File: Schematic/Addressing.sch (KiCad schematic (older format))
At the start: 5 parts, among them IC10 74LS593, IC11 74HCT251, IC7 74HCT574, IC8 74HCT574, IC9 74LS593

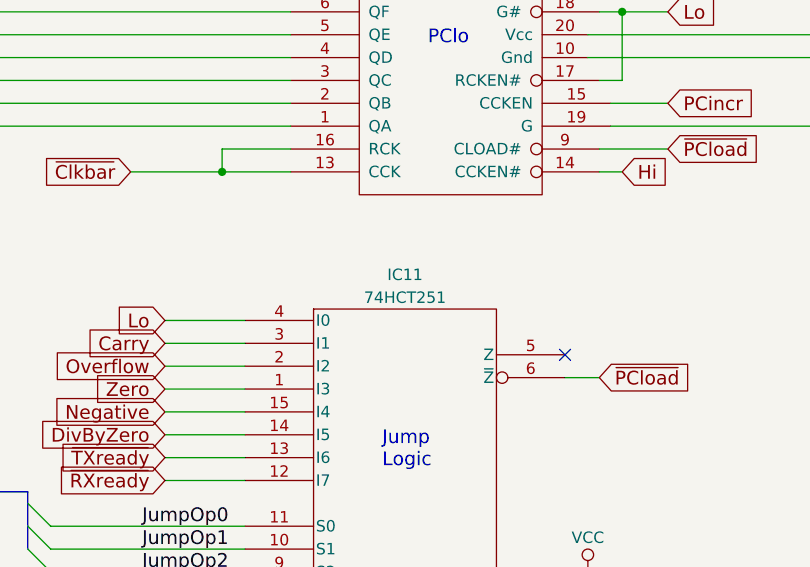
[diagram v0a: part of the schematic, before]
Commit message: Brought the PCB up to date with the new schematic, and tested the RAM with a test program.
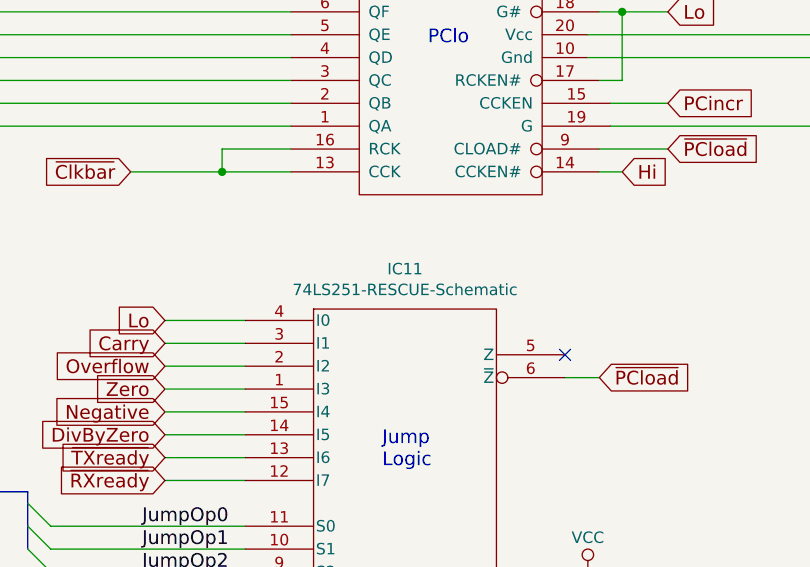
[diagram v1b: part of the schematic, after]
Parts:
- IC11: value 74HCT251 -> 74LS251-RESCUE-Schematic; footprint Housings_DIP:DIP-16_W7.62mm_Socket -> Package_DIP:DIP-16_W7.62mm_Socket
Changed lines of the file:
@@
 Text GLabel 7800 1350 2    60   Input ~ 0
 ~Reset
-$Comp
-L Schematic-rescue:74LS251-RESCUE-Schematic U?
-U 1 1 5CA1932F
-P 6150 5400
-AR Path="/5CA1932F" Ref="U?"  Part="1"
-AR Path="/5C985077/5CA1932F" Ref="IC11"  Part="1"
-F 0 "IC11" H 6150 6250 50  0000 C CNN
-F 1 "74HCT251" H 6150 6150 50  0000 C CNN
-F 2 "Housings_DIP:DIP-16_W7.62mm_Socket" H 6150 5400 50  0001 C CNN
-F 3 "" H 6150 5400 50  0001 C CNN
-	1    6150 5400
-	1    0    0    -1
-$EndComp
 Wire Wire Line
 	6950 5900 6950 5850
@@
 Wire Wire Line
 	7050 2550 7050 3200
+$Comp
+L Schematic-rescue:74LS251-RESCUE-Schematic IC11
+U 1 1 5CDB88DB
+P 6150 5400
+F 0 "IC11" H 6150 6275 50  0000 C CNN
+F 1 "74LS251-RESCUE-Schematic" H 6150 6184 50  0000 C CNN
+F 2 "Package_DIP:DIP-16_W7.62mm_Socket" H 6150 5400 50  0001 C CNN
+F 3 "" H 6150 5400 50  0001 C CNN
+	1    6150 5400
+	1    0    0    -1
+$EndComp
 Wire Bus Line
 	4500 5500 4500 5750

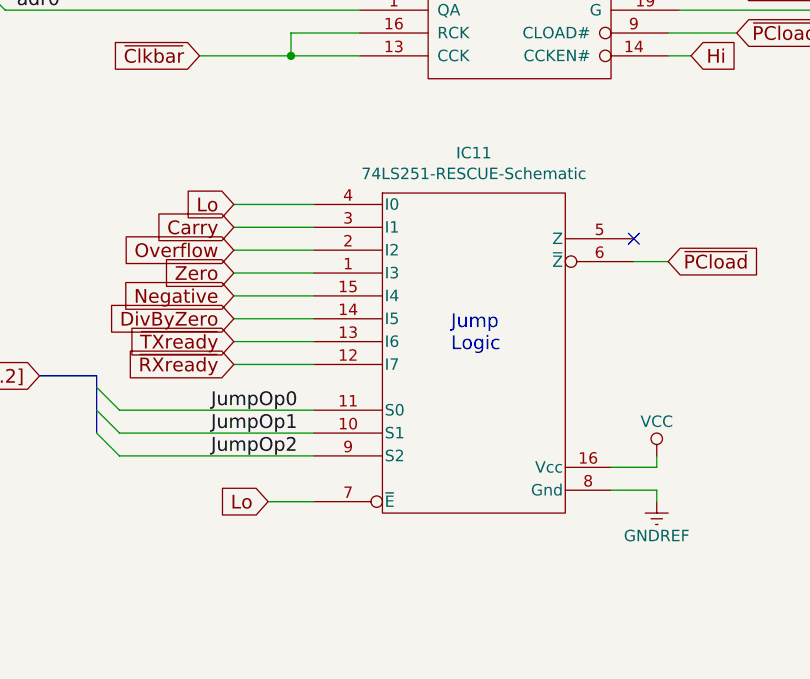
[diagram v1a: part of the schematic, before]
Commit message: I've updated the schematic and the PCB to have the 74HCT151 chip.
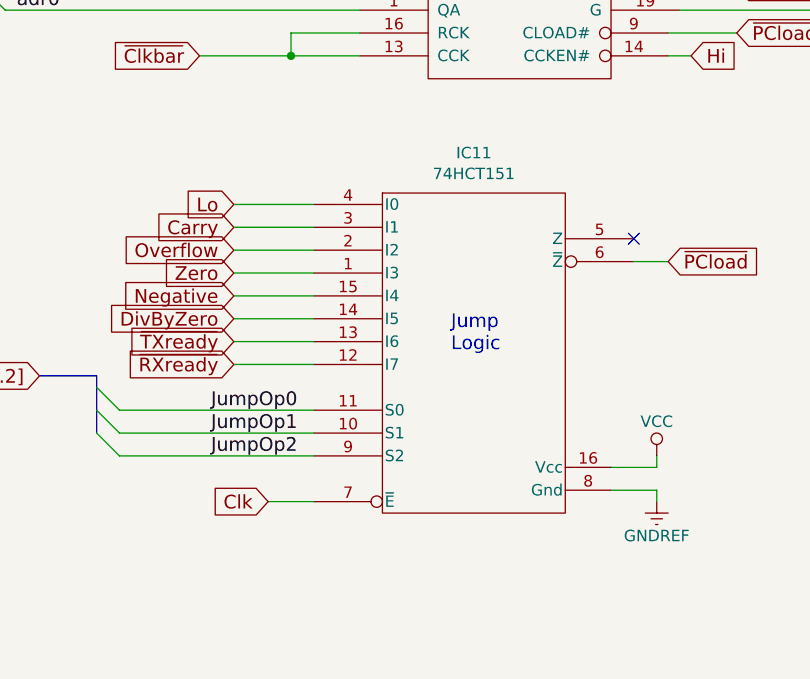
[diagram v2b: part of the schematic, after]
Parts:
- IC11: value 74LS251-RESCUE-Schematic -> 74HCT151
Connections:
- net Lo: no longer IC11.7 (~E)
- new net Clk: IC11.7 (~E)
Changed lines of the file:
@@
 Text GLabel 7300 3400 2    60   Input ~ 0
-Lo
-Text GLabel 5250 6050 0    60   Input ~ 0
 Lo
 Wire Wire Line
@@
 P 6150 5400
 F 0 "IC11" H 6150 6275 50  0000 C CNN
-F 1 "74LS251-RESCUE-Schematic" H 6150 6184 50  0000 C CNN
+F 1 "74HCT151" H 6150 6184 50  0000 C CNN
 F 2 "Package_DIP:DIP-16_W7.62mm_Socket" H 6150 5400 50  0001 C CNN
 F 3 "" H 6150 5400 50  0001 C CNN
@@
 Wire Bus Line
 	1950 1350 1950 4900
+Text GLabel 5250 6050 0    60   Input ~ 0
+Clk
 $EndSCHEMATC
